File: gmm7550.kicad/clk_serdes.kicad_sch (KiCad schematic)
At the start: 50 parts, among them U1 CCGM1A1, U2 CDCE6214, Y1 NX3225SA

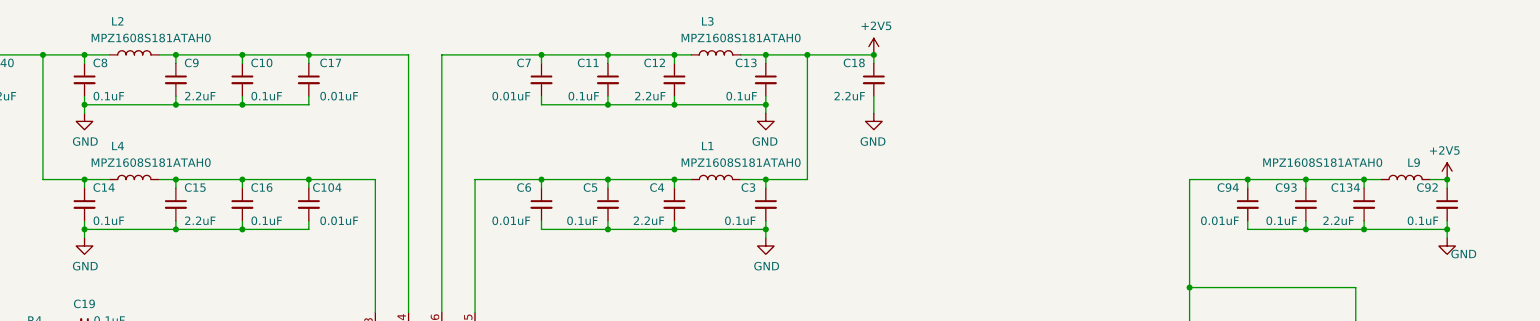
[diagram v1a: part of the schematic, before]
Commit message: Update designs to KiCad v7
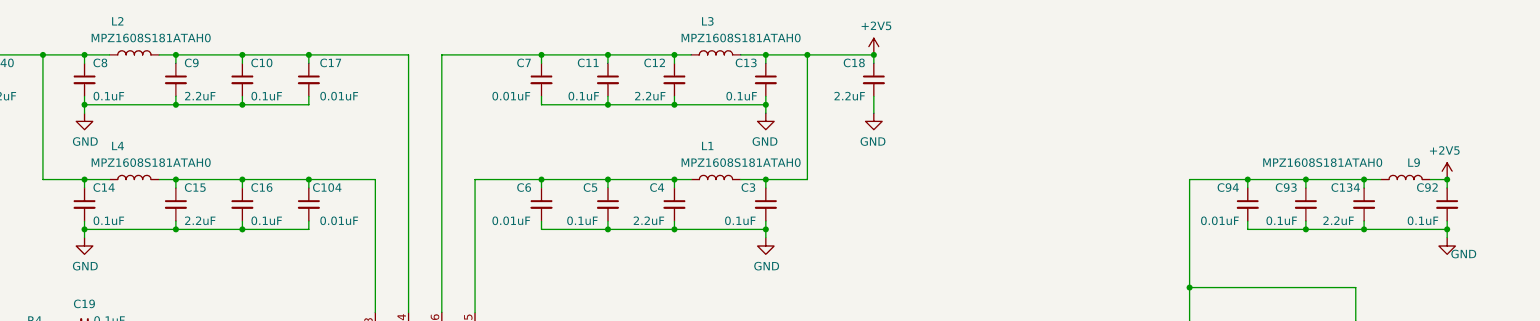
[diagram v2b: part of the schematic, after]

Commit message: Update copyright years and increment revision
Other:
- note added: "Copyright (c) 2020-2024 Anton Kuzmin Licensed under CERN-OHL-P v2 https://github.com/gmm-7550/"
- note removed: "Copyright (c) 2020-2022 Anton Kuzmin Licensed under CERN-OHL-P v2 https://github.com/ak-fau/gmm7550.git"
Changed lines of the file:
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@@
   (title_block
     (title "GateMate FPGA Module: GMM-7550")
-    (date "2022-04-24")
-    (rev "2.1")
+    (date "2022-04-27")
+    (rev "2.2")
   )
   (junction (at 152.4 33.02) (diameter 0) (color 0 0 0 0)
@@
     (stroke (width 0) (type default))
   )
-  (text "Copyright (c) 2020-2022  Anton Kuzmin\nLicensed under CERN-OHL-P v2\nhttps://github.com/ak-fau/gmm7550.git"
+  (text "Copyright (c) 2020-2024  Anton Kuzmin\nLicensed under CERN-OHL-P v2\nhttps://github.com/gmm-7550/"
     (at 198.12 179.07 0)
     (effects (font (size 2.54 2.54)) (justify left bottom))
